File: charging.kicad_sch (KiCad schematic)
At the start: 4 parts, among them U3 MCP73811T-420I-OT

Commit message: Start routing antennna
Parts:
- removed U3: MCP73811T-420I-OT, Package_TO_SOT_SMD:SOT-23-5, symbol Battery_Management:MCP73811T-420I-OT
- added C19, C20: 4.7uF, symbol Device:C
- added D43, D44: LED, symbol Device:LED
- added R5, R7: 1.5k, symbol Device:R
- added R6: 3.9k, symbol Device:R
- added R8: 47k, symbol Device:R
- added U2: BQ24075RGT, Package_DFN_QFN:VQFN-16-1EP_3x3mm_P0.5mm_EP1.6x1.6mm, symbol Battery_Management:BQ24075RGT
- C18: footprint Capacitor_SMD:C_0603_1608Metric -> (none)
- R3: value 5k -> 10k; footprint Resistor_SMD:R_0603_1608Metric -> (none)
- R4: value 10k -> 1.5k; footprint Resistor_SMD:R_0603_1608Metric -> (none)
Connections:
- net GND: now also R3.2, R4.1, C19.2, C20.2, R6.1, R7.1, R8.1, U2.17 (VSS), U2.4 (~{CE}), U2.5 (EN2), U2.7 (~{PGOOD}), U2.8 (VSS); no longer R3.1
- net VBAT: now also C18.1, U2.2 (BAT), U2.3 (BAT)
- net VBUS: now also C20.1, U2.13 (IN)
- net at R4.2: now also D43.1 (K)
- new net: R6.2, U2.16 (ISET)
- new net: R8.2, U2.14 (TMR)
- new net: R7.2, U2.12 (ILIM)
- new net: D44.1 (K), R5.2
- new net: R3.1, U2.1 (TS)
- new net: R5.1, U2.9 (~{CHG})
- new net SYSOFF: U2.15 (SYSOFF)
- new net VDDH: C19.1, D43.2 (A), D44.2 (A), U2.10 (OUT), U2.11 (OUT), U2.6 (EN1)

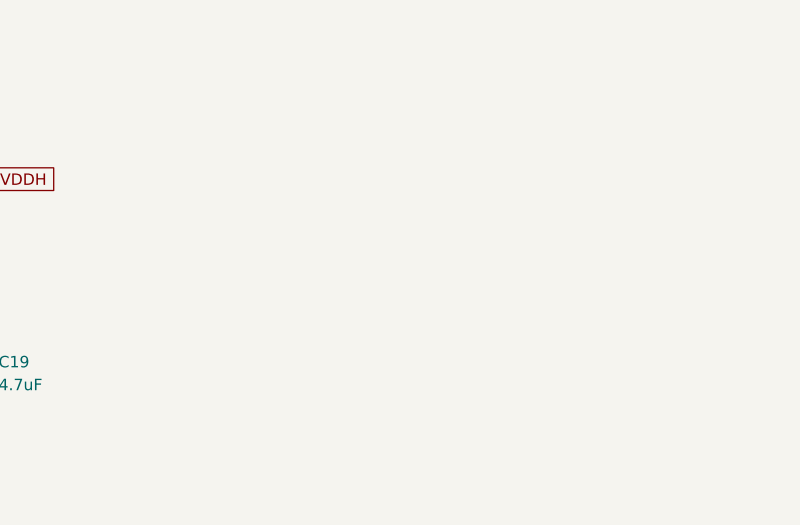
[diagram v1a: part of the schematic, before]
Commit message: Change board shape
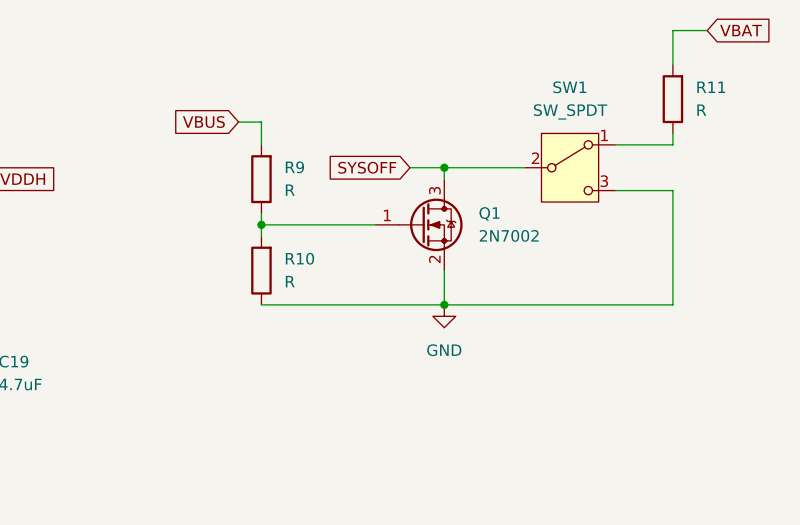
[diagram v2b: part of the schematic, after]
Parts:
- added Q1: 2N7002, Package_TO_SOT_SMD:SOT-23, symbol Transistor_FET:2N7002
- added R10, R11, R9: R, symbol Device:R
- added SW1: SW_SPDT, symbol Switch:SW_SPDT
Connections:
- net GND: now also Q1.2 (S), R10.1, SW1.3 (C)
- net SYSOFF: now also Q1.3 (D), SW1.2 (B)
- net VBAT: now also R11.2
- net VBUS: now also R9.2
- new net: Q1.1 (G), R10.2, R9.1
- new net: R11.1, SW1.1 (A)
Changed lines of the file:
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@@
     (rev "0")
   )
+  (junction (at 171.45 76.2) (diameter 0) (color 0 0 0 0)
+  )
   (junction (at 102.87 99.06) (diameter 0) (color 0 0 0 0)
   )
@@
   (junction (at 33.02 99.06) (diameter 0) (color 0 0 0 0)
   )
+  (junction (at 191.77 85.09) (diameter 0) (color 0 0 0 0)
+  )
+  (junction (at 191.77 69.85) (diameter 0) (color 0 0 0 0)
+  )
   (junction (at 102.87 78.74) (diameter 0) (color 0 0 0 0)
   )
@@
   (junction (at 118.11 71.12) (diameter 0) (color 0 0 0 0)
   )
+  (wire (pts (xy 217.17 85.09) (xy 191.77 85.09))
+    (stroke (width 0) (type default))
+  )
   (wire (pts (xy 33.02 99.06) (xy 36.83 99.06))
     (stroke (width 0) (type default))
@@
     (stroke (width 0) (type default))
   )
+  (wire (pts (xy 191.77 69.85) (xy 200.66 69.85))
+    (stroke (width 0) (type default))
+  )
   (wire (pts (xy 36.83 78.74) (xy 36.83 91.44))
     (stroke (width 0) (type default))
@@
     (stroke (width 0) (type default))
   )
+  (wire (pts (xy 210.82 72.39) (xy 217.17 72.39))
+    (stroke (width 0) (type default))
+  )
   (wire (pts (xy 86.36 91.44) (xy 128.27 91.44))
     (stroke (width 0) (type default))
   )
+  (wire (pts (xy 210.82 67.31) (xy 217.17 67.31))
+    (stroke (width 0) (type default))
+  )
   (wire (pts (xy 54.61 91.44) (xy 60.96 91.44))
     (stroke (width 0) (type default))
@@
     (stroke (width 0) (type default))
   )
+  (wire (pts (xy 171.45 76.2) (xy 184.15 76.2))
+    (stroke (width 0) (type default))
+  )
+  (wire (pts (xy 191.77 85.09) (xy 191.77 81.28))
+    (stroke (width 0) (type default))
+  )
   (wire (pts (xy 86.36 88.9) (xy 102.87 88.9))
     (stroke (width 0) (type default))
@@
     (stroke (width 0) (type default))
   )
+  (wire (pts (xy 187.96 69.85) (xy 191.77 69.85))
+    (stroke (width 0) (type default))
+  )
+  (wire (pts (xy 191.77 69.85) (xy 191.77 71.12))
+    (stroke (width 0) (type default))
+  )
   (wire (pts (xy 118.11 71.12) (xy 118.11 72.39))
     (stroke (width 0) (type default))
@@
     (stroke (width 0) (type default))
   )
+  (wire (pts (xy 171.45 85.09) (xy 191.77 85.09))
+    (stroke (width 0) (type default))
+  )
   (wire (pts (xy 99.06 99.06) (xy 102.87 99.06))
     (stroke (width 0) (type default))
@@
     (stroke (width 0) (type default))
   )
+  (wire (pts (xy 171.45 74.93) (xy 171.45 76.2))
+    (stroke (width 0) (type default))
+  )
+  (wire (pts (xy 217.17 67.31) (xy 217.17 66.04))
+    (stroke (width 0) (type default))
+  )
   (wire (pts (xy 36.83 99.06) (xy 45.72 99.06))
     (stroke (width 0) (type default))
@@
     (stroke (width 0) (type default))
   )
+  (wire (pts (xy 168.91 64.77) (xy 171.45 64.77))
+    (stroke (width 0) (type default))
+  )
+  (wire (pts (xy 217.17 54.61) (xy 220.98 54.61))
+    (stroke (width 0) (type default))
+  )
   (wire (pts (xy 33.02 83.82) (xy 60.96 83.82))
+    (stroke (width 0) (type default))
+  )
+  (wire (pts (xy 217.17 58.42) (xy 217.17 54.61))
+    (stroke (width 0) (type default))
+  )
+  (wire (pts (xy 171.45 76.2) (xy 171.45 77.47))
+    (stroke (width 0) (type default))
+  )
+  (wire (pts (xy 171.45 64.77) (xy 171.45 67.31))
+    (stroke (width 0) (type default))
+  )
+  (wire (pts (xy 217.17 72.39) (xy 217.17 85.09))
     (stroke (width 0) (type default))
   )
@@
     )
   )
+  (global_label "SYSOFF" (shape input) (at 187.96 69.85 180) (fields_autoplaced)
+    (effects (font (size 1.27 1.27)) (justify right))
+    (property "Intersheetrefs" "${INTERSHEET_REFS}" (at 177.9595 69.85 0)
+      (effects (font (size 1.27 1.27)) (justify right) hide)
+    )
+  )
   (global_label "VDDH" (shape input) (at 140.97 71.12 0) (fields_autoplaced)
     (effects (font (size 1.27 1.27)) (justify left))
@@
     )
   )
+  (global_label "VBAT" (shape input) (at 220.98 54.61 0) (fields_autoplaced)
+    (effects (font (size 1.27 1.27)) (justify left))
+    (property "Intersheetrefs" "${INTERSHEET_REFS}" (at 228.38 54.61 0)
+      (effects (font (size 1.27 1.27)) (justify left) hide)
+    )
+  )
   (global_label "VDDH" (shape input) (at 60.96 81.28 180) (fields_autoplaced)
     (effects (font (size 1.27 1.27)) (justify right))
@@
     )
   )
+  (global_label "VBUS" (shape input) (at 168.91 64.77 180) (fields_autoplaced)
+    (effects (font (size 1.27 1.27)) (justify right))
+    (property "Intersheetrefs" "${INTERSHEET_REFS}" (at 161.0262 64.77 0)
+      (effects (font (size 1.27 1.27)) (justify right) hide)
+    )
+  )
   (symbol (lib_id "Device:R") (at 54.61 95.25 180) (unit 1)
     (in_bom yes) (on_board yes) (dnp no) (fields_autoplaced)
@@
         (path "/a3795772-e8b2-4a24-8aa0-5a93e6e5ac56/c2fac475-eefc-4fa7-89e3-f138d1e57553"
           (reference "D44") (unit 1)
+        )
+      )
+    )
+  )
+  (symbol (lib_id "Device:R") (at 171.45 71.12 180) (unit 1)
+    (in_bom yes) (on_board yes) (dnp no) (fields_autoplaced)
+    (property "Reference" "R9" (at 173.99 69.85 0)
+      (effects (font (size 1.27 1.27)) (justify right))
+    )
+    (property "Value" "R" (at 173.99 72.39 0)
+      (effects (font (size 1.27 1.27)) (justify right))
+    )
+    (property "Footprint" "" (at 173.228 71.12 90)
+      (effects (font (size 1.27 1.27)) hide)
+    )
+    (property "Datasheet" "~" (at 171.45 71.12 0)
+      (effects (font (size 1.27 1.27)) hide)
+    )
+    (pin "2")
+    (pin "1")
+    (instances
+      (project "keyboard"
+        (path "/a3795772-e8b2-4a24-8aa0-5a93e6e5ac56/c2fac475-eefc-4fa7-89e3-f138d1e57553"
+          (reference "R9") (unit 1)
+        )
+      )
+    )
+  )
+  (symbol (lib_id "Switch:SW_SPDT") (at 205.74 69.85 0) (unit 1)
+    (in_bom yes) (on_board yes) (dnp no) (fields_autoplaced)
+    (property "Reference" "SW1" (at 205.74 60.96 0)
+      (effects (font (size 1.27 1.27)))
+    )
+    (property "Value" "SW_SPDT" (at 205.74 63.5 0)
+      (effects (font (size 1.27 1.27)))
+    )
+    (property "Footprint" "" (at 205.74 69.85 0)
+      (effects (font (size 1.27 1.27)) hide)
+    )
+    (property "Datasheet" "~" (at 205.74 77.47 0)
+      (effects (font (size 1.27 1.27)) hide)
+    )
+    (pin "1")
+    (pin "3")
+    (pin "2")
+    (instances
+      (project "keyboard"
+        (path "/a3795772-e8b2-4a24-8aa0-5a93e6e5ac56/c2fac475-eefc-4fa7-89e3-f138d1e57553"
+          (reference "SW1") (unit 1)
         )
       )
@@
     )
   )
+  (symbol (lib_id "Device:R") (at 217.17 62.23 180) (unit 1)
+    (in_bom yes) (on_board yes) (dnp no) (fields_autoplaced)
+    (property "Reference" "R11" (at 219.71 60.96 0)
+      (effects (font (size 1.27 1.27)) (justify right))
+    )
+    (property "Value" "R" (at 219.71 63.5 0)
+      (effects (font (size 1.27 1.27)) (justify right))
+    )
+    (property "Footprint" "" (at 218.948 62.23 90)
+      (effects (font (size 1.27 1.27)) hide)
+    )
+    (property "Datasheet" "~" (at 217.17 62.23 0)
+      (effects (font (size 1.27 1.27)) hide)
+    )
+    (pin "2")
+    (pin "1")
+    (instances
+      (project "keyboard"
+        (path "/a3795772-e8b2-4a24-8aa0-5a93e6e5ac56/c2fac475-eefc-4fa7-89e3-f138d1e57553"
+          (reference "R11") (unit 1)
+        )
+      )
+    )
+  )
   (symbol (lib_id "Device:R") (at 92.71 83.82 90) (unit 1)
     (in_bom yes) (on_board yes) (dnp no) (fields_autoplaced)
@@
     )
   )
+  (symbol (lib_id "Device:R") (at 171.45 81.28 180) (unit 1)
+    (in_bom yes) (on_board yes) (dnp no) (fields_autoplaced)
+    (property "Reference" "R10" (at 173.99 80.01 0)
+      (effects (font (size 1.27 1.27)) (justify right))
+    )
+    (property "Value" "R" (at 173.99 82.55 0)
+      (effects (font (size 1.27 1.27)) (justify right))
+    )
+    (property "Footprint" "" (at 173.228 81.28 90)
+      (effects (font (size 1.27 1.27)) hide)
+    )
+    (property "Datasheet" "~" (at 171.45 81.28 0)
+      (effects (font (size 1.27 1.27)) hide)
+    )
+    (pin "2")
+    (pin "1")
+    (instances
+      (project "keyboard"
+        (path "/a3795772-e8b2-4a24-8aa0-5a93e6e5ac56/c2fac475-eefc-4fa7-89e3-f138d1e57553"
+          (reference "R10") (unit 1)
+        )
+      )
+    )
+  )
+  (symbol (lib_id "power:GND") (at 191.77 85.09 0) (unit 1)
+    (in_bom yes) (on_board yes) (dnp no) (fields_autoplaced)
+    (property "Reference" "#PWR017" (at 191.77 91.44 0)
+      (effects (font (size 1.27 1.27)) hide)
+    )
+    (property "Value" "GND" (at 191.77 90.17 0)
+      (effects (font (size 1.27 1.27)))
+    )
+    (property "Footprint" "" (at 191.77 85.09 0)
+      (effects (font (size 1.27 1.27)) hide)
+    )
+    (property "Datasheet" "" (at 191.77 85.09 0)
+      (effects (font (size 1.27 1.27)) hide)
+    )
+    (pin "1")
+    (instances
+      (project "keyboard"
+        (path "/a3795772-e8b2-4a24-8aa0-5a93e6e5ac56/c2fac475-eefc-4fa7-89e3-f138d1e57553"
+          (reference "#PWR017") (unit 1)
+        )
+      )
+    )
+  )
   (symbol (lib_id "Device:LED") (at 118.11 76.2 90) (unit 1)
     (in_bom yes) (on_board yes) (dnp no) (fields_autoplaced)
@@
         )
       )
+    )
+  )
+  (symbol (lib_id "Transistor_FET:2N7002") (at 189.23 76.2 0) (unit 1)
+    (in_bom yes) (on_board yes) (dnp no) (fields_autoplaced)
+    (property "Reference" "Q1" (at 195.58 74.93 0)
+      (effects (font (size 1.27 1.27)) (justify left))
+    )
+    (property "Value" "2N7002" (at 195.58 77.47 0)
+      (effects (font (size 1.27 1.27)) (justify left))
+    )
+    (property "Footprint" "Package_TO_SOT_SMD:SOT-23" (at 194.31 78.105 0)
+      (effects (font (size 1.27 1.27) italic) (justify left) hide)
+    )
+    (property "Datasheet" "https://www.onsemi.com/pub/Collateral/NDS7002A-D.PDF" (at 194.31 80.01 0)
+      (effects (font (size 1.27 1.27)) (justify left) hide)
+    )
+    (pin "1")
+    (pin "3")
+    (pin "2")
+    (instances
+      (project "keyboard"
+        (path "/a3795772-e8b2-4a24-8aa0-5a93e6e5ac56/c2fac475-eefc-4fa7-89e3-f138d1e57553"
+          (reference "Q1") (unit 1)
+        )
+      )
